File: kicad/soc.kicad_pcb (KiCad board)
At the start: 2 copper layers, 76.2 x 63.5 mm, 60 parts, among them J1 Line Out, J2 PS/2 Keyboard, J3 DB9, J4 Line In, J5 Headphone, P1 LED MATRIX, P2 ALTERA_DE1_GPIO, P3 IO, U1 SSM2603, U2 DS3234, U3 speakjet, U4 MAX3232

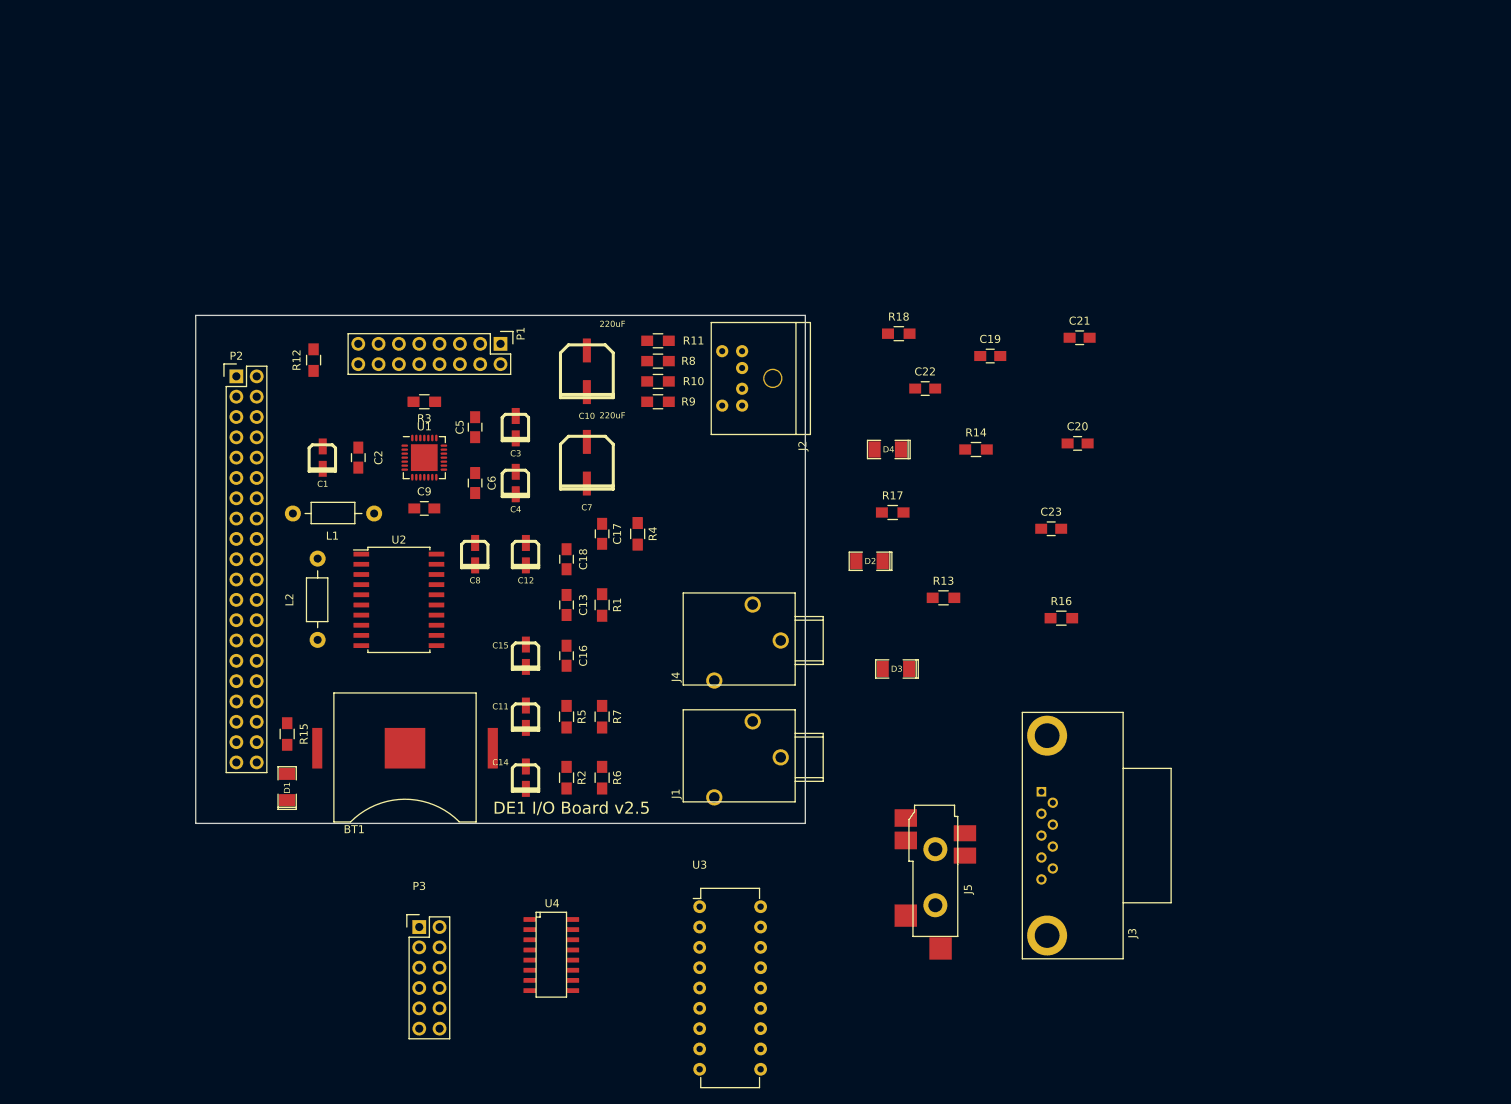
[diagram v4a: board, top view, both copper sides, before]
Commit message: adding mic input
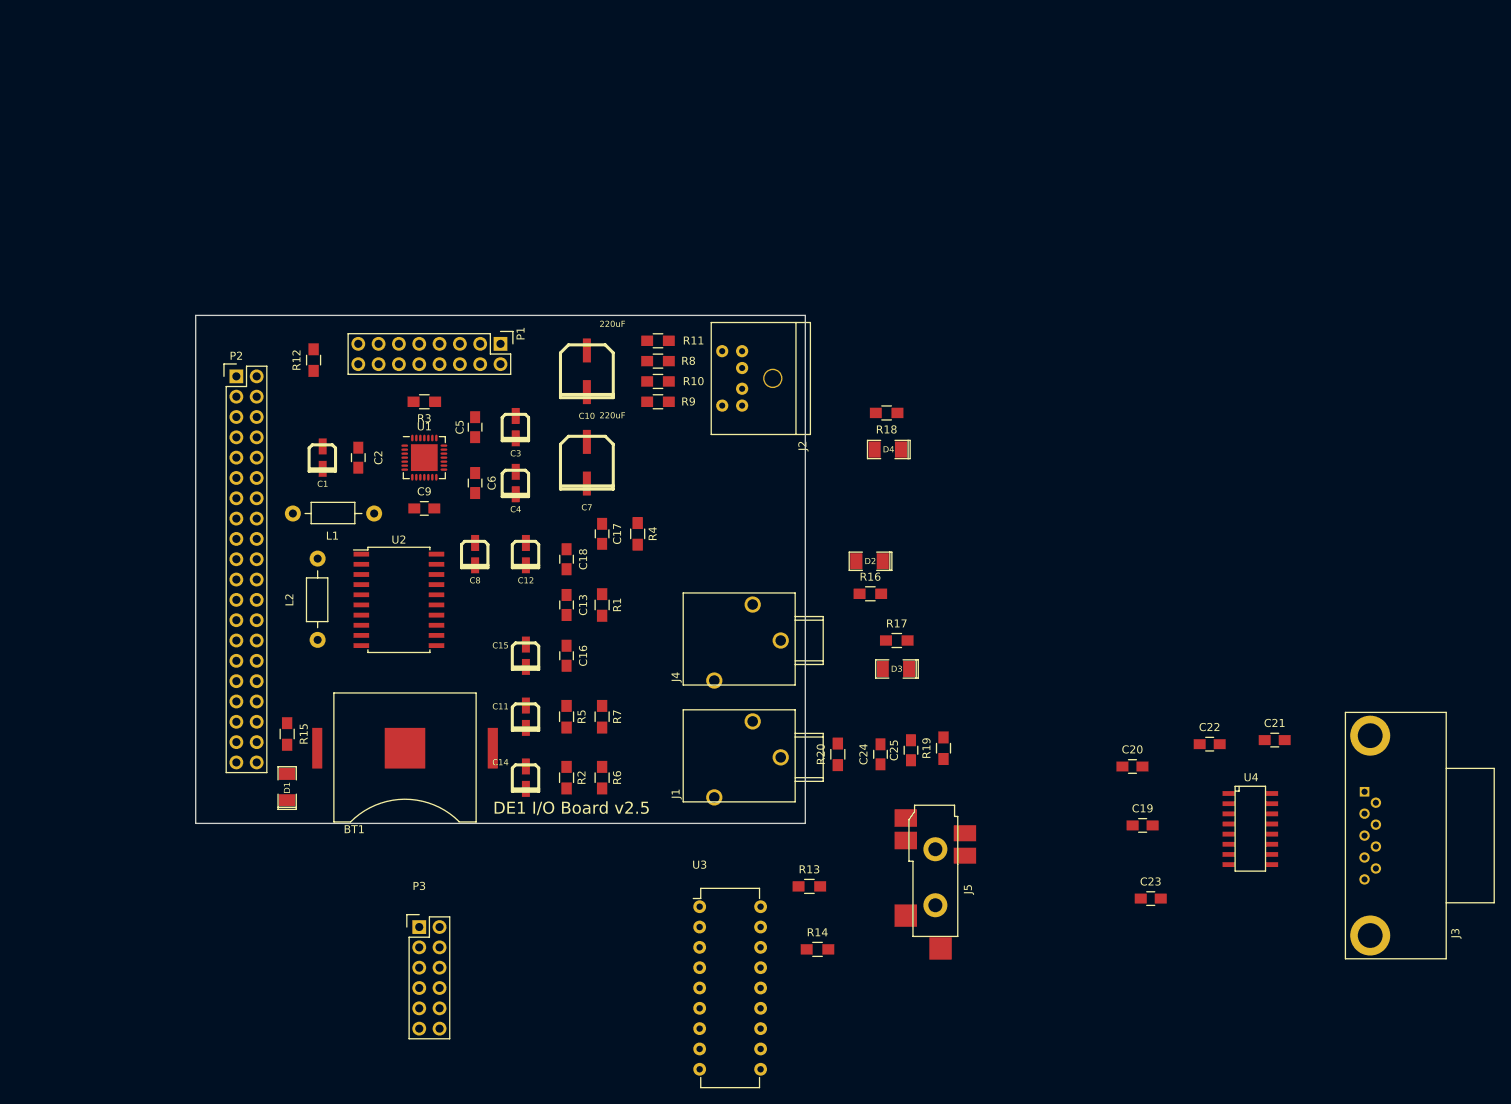
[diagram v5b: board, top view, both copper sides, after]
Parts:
- added C24: 1uF, Capacitors_SMD:C_0805_HandSoldering, F.Cu at (126.2, 115.8)
- added C25: 220pF, Capacitors_SMD:C_0805_HandSoldering, F.Cu at (130.0, 115.3)
- added R19: 47k, Resistors_SMD:R_0805_HandSoldering, F.Cu at (134.1, 115.1)
- added R20: 100, Resistors_SMD:R_0805_HandSoldering, F.Cu at (120.9, 115.8)
- moved U4 88.8 mm to (172.5, 125.2)
- moved R14 65.5 mm to (118.4, 140.2)
- moved C19 61.7 mm to (159.0, 124.7)
- moved C22 56.9 mm to (167.4, 114.6)
- moved C21 55.9 mm to (175.5, 114.0)
- moved C23 47.9 mm to (160.0, 133.9)
- moved C20 41.0 mm to (157.7, 117.3)
- moved J3 40.4 mm to (187.5, 126.0)
- moved R13 39.8 mm to (117.3, 132.3)
- moved R16 24.1 mm to (125.0, 95.8)
- moved R17 16.0 mm to (128.3, 101.6)
- moved R18 10.0 mm to (127.0, 73.2), turned to 180 degrees
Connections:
- J2 pad 2: Net-(J2-Pad2) -> (no net)
- J2 pad 6: Net-(J2-Pad6) -> (no net)
- J3 pad 1: Net-(J3-Pad1) -> (no net)
- J3 pad 4: Net-(J3-Pad4) -> (no net)
- J3 pad 6: Net-(J3-Pad6) -> (no net)
- P1 pad 12: Net-(P1-Pad12) -> (no net)
- P2 pad 36: Net-(P2-Pad36) -> (no net)
- P2 pad 37: Net-(P2-Pad37) -> (no net)
- P2 pad 38: Net-(P2-Pad38) -> (no net)
- P2 pad 39: Net-(P2-Pad39) -> (no net)
- P2 pad 40: Net-(P2-Pad40) -> (no net)
- U1 pad 16: Net-(R14-Pad2) -> Net-(C11-Pad1)
- U1 pad 17: Net-(C11-Pad1) -> Net-(R14-Pad2)
- U1 pad 2: Net-(U1-Pad2) -> (no net)
- U1 pad 23: Net-(C12-Pad1) -> Net-(C15-Pad1)
- U1 pad 24: Net-(C15-Pad1) -> Net-(C12-Pad1)
- U1 pad 6: Net-(U1-Pad6) -> (no net)
- U2 pad 10: Net-(U2-Pad10) -> (no net)
- U2 pad 11: Net-(U2-Pad11) -> (no net)
- U2 pad 12: Net-(U2-Pad12) -> (no net)
- U2 pad 13: Net-(U2-Pad13) -> (no net)
- U2 pad 14: Net-(U2-Pad14) -> (no net)
- U2 pad 2: Net-(U2-Pad2) -> (no net)
- U2 pad 3: Net-(U2-Pad3) -> (no net)
- U2 pad 5: Net-(U2-Pad5) -> (no net)
- U2 pad 7: Net-(U2-Pad7) -> (no net)
- U2 pad 8: Net-(U2-Pad8) -> (no net)
- U2 pad 9: Net-(U2-Pad9) -> (no net)
- U3 pad 15: /Serial1_busy -> (no net)
- U3 pad 17: Net-(U3-Pad17) -> (no net)
- U4 pad 10: /Serial0_CTS -> (no net)
- U4 pad 9: /Serial0_RTS -> (no net)

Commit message: board layout progress, new SMT audio jacks
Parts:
- J1, J4: footprint mstock-pretty:SJI-3513N -> mstock-pretty:SJ-352X-SMT
- moved C20 138.3 mm to (50.5, 30.0)
- moved C21 138.3 mm to (68.3, 26.7)
- moved C23 138.3 mm to (52.8, 46.5)
- moved C19 138.3 mm to (51.8, 37.3)
- moved C22 138.3 mm to (60.2, 27.2)
- moved J3 111.4 mm to (93.7, 65.8), turned to 0 degrees
- moved R18 103.7 mm to (48.5, 141.0)
- moved D4 98.6 mm to (48.0, 136.4)
- moved U4 93.2 mm to (93.2, 76.2), turned to 0 degrees
- moved R16 92.5 mm to (53.1, 153.9)
- moved D2 91.3 mm to (54.4, 149.6)
- moved R17 83.0 mm to (55.9, 142.2)
- moved D3 78.5 mm to (56.9, 137.9)
- moved R14 68.8 mm to (74.9, 86.9), turned to 180 degrees
- moved C24 41.3 mm to (114.6, 76.2), turned to 180 degrees
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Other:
- board size 76.2 x 63.5 mm -> 91.4 x 73.7 mm

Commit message: finish pcb rev
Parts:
- moved D4 73.5 mm to (120.7, 125.5), turned to 270 degrees
- moved C20 70.2 mm to (95.0, 84.3)
- moved D2 63.0 mm to (112.5, 125.5), turned to 270 degrees
- moved D3 61.0 mm to (116.6, 125.5), turned to 270 degrees
- moved C19 60.3 mm to (89.7, 84.3)
- moved C22 56.9 mm to (84.8, 78.5), turned to 270 degrees
- moved D1 56.7 mm to (108.5, 125.5)
- moved R18 54.6 mm to (96.0, 114.0), turned to 0 degrees
- moved R16 53.4 mm to (96.0, 122.2)
- moved C21 50.3 mm to (88.1, 72.9)
- moved C23 50.0 mm to (95.2, 72.9)
- moved P3 48.1 mm to (72.1, 89.4)
- moved R17 46.8 mm to (96.0, 118.1)
- moved R15 45.9 mm to (96.0, 126.5), turned to 0 degrees
- moved C10 17.4 mm to (99.8, 92.5)
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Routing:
- net GND: track 0.00 -> 485.1 mm, vias 0 -> 1
- net +3V3: track 0.00 -> 235.6 mm
- net /Serial1_TX: track 0.00 -> 113.0 mm
- net /Kbd_data: track 0.00 -> 94.0 mm
- net +5V: track 0.00 -> 93.1 mm
- net /Kbd_clk: track 0.00 -> 89.5 mm
- net Net-(C11-Pad1): track 0.00 -> 71.5 mm
- net /Serial0_RX: track 0.00 -> 63.9 mm, vias 0 -> 2
- net Net-(BT1-Pad1): track 0.00 -> 63.9 mm
- net /Serial0_TX: track 0.00 -> 63.0 mm, vias 0 -> 2
- net /SCLK: track 0.00 -> 63.0 mm, vias 0 -> 1
- net /~RESET: track 0.00 -> 61.5 mm
- net Net-(C24-Pad2): track 0.00 -> 57.9 mm
- net Net-(C8-Pad1): track 0.00 -> 57.2 mm, vias 0 -> 1
- net /SDIN: track 0.00 -> 54.1 mm, vias 0 -> 2
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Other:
- board text added: "Bexkat Systems LLC 2017 www.bexkat.com"
- board text removed: "Bexkat Systems LLC 2016 www.bexkat.com"
